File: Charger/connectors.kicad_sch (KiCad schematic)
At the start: 0 parts

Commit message: charger WIP
Most footprints assigned, shunt drawn in schem
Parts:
- added J3: Conn_01x10, symbol Connector_Generic:Conn_01x10
- added J4, J5: Conn_01x03, Connector_Molex:Molex_Micro-Fit_3.0_43650-0315_1x03_P3.00mm_Vertical, symbol Connector_Generic:Conn_01x03
- added J6, J7: Conn_01x02, Connector_Molex:Molex_Micro-Fit_3.0_43650-0215_1x02_P3.00mm_Vertical, symbol Connector_Generic:Conn_01x02
- added P1: IEC_60320_C13_Plug, symbol Connector:IEC_60320_C13_Plug
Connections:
- new net +12V: J3.6 (Pin_6), J6.2 (Pin_2)
- new net AMP_GND: J5.3 (Pin_3)
- new net AMP_SIGNAL: J5.2 (Pin_2)
- new net AMP_VCC: J5.1 (Pin_1)
- new net AMS_ERR: J3.3 (Pin_3)
- new net CANH: J3.8 (Pin_8)
- new net CANL: J3.9 (Pin_9)
- new net CAN_SHIELD: J3.10 (Pin_10)
- new net CHARGING_ENABLE: J6.1 (Pin_1)
- new net GND: J3.7 (Pin_7)
- new net GNDPWR: P1.3 (PE)
- new net IMD_ERR: J3.4 (Pin_4)
- new net LIVE: P1.2 (L)
- new net NEUT: P1.1 (N)
- new net RSNS+: J7.1 (Pin_1)
- new net RSNS-: J7.2 (Pin_2)
- new net SDC_IN: J3.2 (Pin_2)
- new net SDC_OUT: J3.1 (Pin_1)
- new net TSAL_G: J3.5 (Pin_5)
- new net VOLT_GND: J4.3 (Pin_3)
- new net VOLT_SIGNAL: J4.2 (Pin_2)
- new net VOLT_VCC: J4.1 (Pin_1)
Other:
- note added: "A control"
- note added: "J"
- note added: "MX 1x2"
- note added: "MX 1x3"
- note added: "V control"
- note added: "not fully accurate but sufficent information"

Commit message: Revise charger and HVPDU schematics
Updates the KiCad projects for Charger and Schematics with substantial schematic rework: replaces the AVR ISP header with a dedicated AVR-ISP-6 symbol, adjusts wiring/net labels and power symbols, adds new indicator/connectivity elements, and repositions components in HV iso and connector sheets. The HVPDU sheet is expanded to A3 and reorganized with additional connector/library symbol definitions and updated interconnect mapping. This commit also includes newly generated schematic backups and an exported HVPDU PDF.
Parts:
- added J10, J9: Conn_01x06, symbol Connector_Generic:Conn_01x06
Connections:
- net +12V: now also J10.1 (Pin_1)
- net GND: now also J9.1 (Pin_1), J9.2 (Pin_2), J9.3 (Pin_3), J9.4 (Pin_4), J9.5 (Pin_5), J9.6 (Pin_6)

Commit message: Charger 0.1.0 PCB ready for review
Silkscreen adjustments have not been finished yet
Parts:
- added F2: Fuse, fuse:LittleFuse_462, symbol Device:Fuse
- added H1, H2, H3, H4: MountingHole, MountingHole:MountingHole_4.3mm_M4, symbol Mechanical:MountingHole
- added J11, J12: Conn_01x02, Connector_Molex:Molex_Micro-Fit_3.0_43650-0200_1x02_P3.00mm_Horizontal, symbol Connector_Generic:Conn_01x02
- added J13, J14, J15, J16: Conn_01x02, Connector_Molex:Molex_Micro-Fit_3.0_43650-0215_1x02_P3.00mm_Vertical, symbol Connector_Generic:Conn_01x02
- added J17: Conn_01x02, Connector_JST:JST_XH_B2B-XH-A_1x02_P2.50mm_Vertical, symbol Connector_Generic:Conn_01x02
- J10, J9: footprint (none) -> Connector_Molex:Molex_Micro-Fit_3.0_43650-0615_1x06_P3.00mm_Vertical
- J7: footprint Connector_Molex:Molex_Micro-Fit_3.0_43650-0215_1x02_P3.00mm_Vertical -> Connector_Molex:Molex_Micro-Fit_3.0_43650-0200_1x02_P3.00mm_Horizontal
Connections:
- net +12V: now also J10.2 (Pin_2), J10.3 (Pin_3), J10.4 (Pin_4), J10.5 (Pin_5), J10.6 (Pin_6)
- net CANH: now also J17.2 (Pin_2)
- net CANL: now also J17.1 (Pin_1)
- net RSNS+: now also J7.2 (Pin_2); no longer J7.1 (Pin_1)
- net RSNS-: now also J7.1 (Pin_1); no longer J7.2 (Pin_2)
- net SDC_IN: now also J15.1 (Pin_1), J15.2 (Pin_2)
- new net: F2.1, J11.1 (Pin_1), J11.2 (Pin_2)
- new net CHARGER_ERR_12V: J14.1 (Pin_1), J14.2 (Pin_2)
- new net HV_ON: J13.1 (Pin_1), J13.2 (Pin_2)
- new net HV_RELAY_AUX: J16.1 (Pin_1), J16.2 (Pin_2)
- new net TS+: F2.2
- new net TS-: J12.1 (Pin_1), J12.2 (Pin_2)

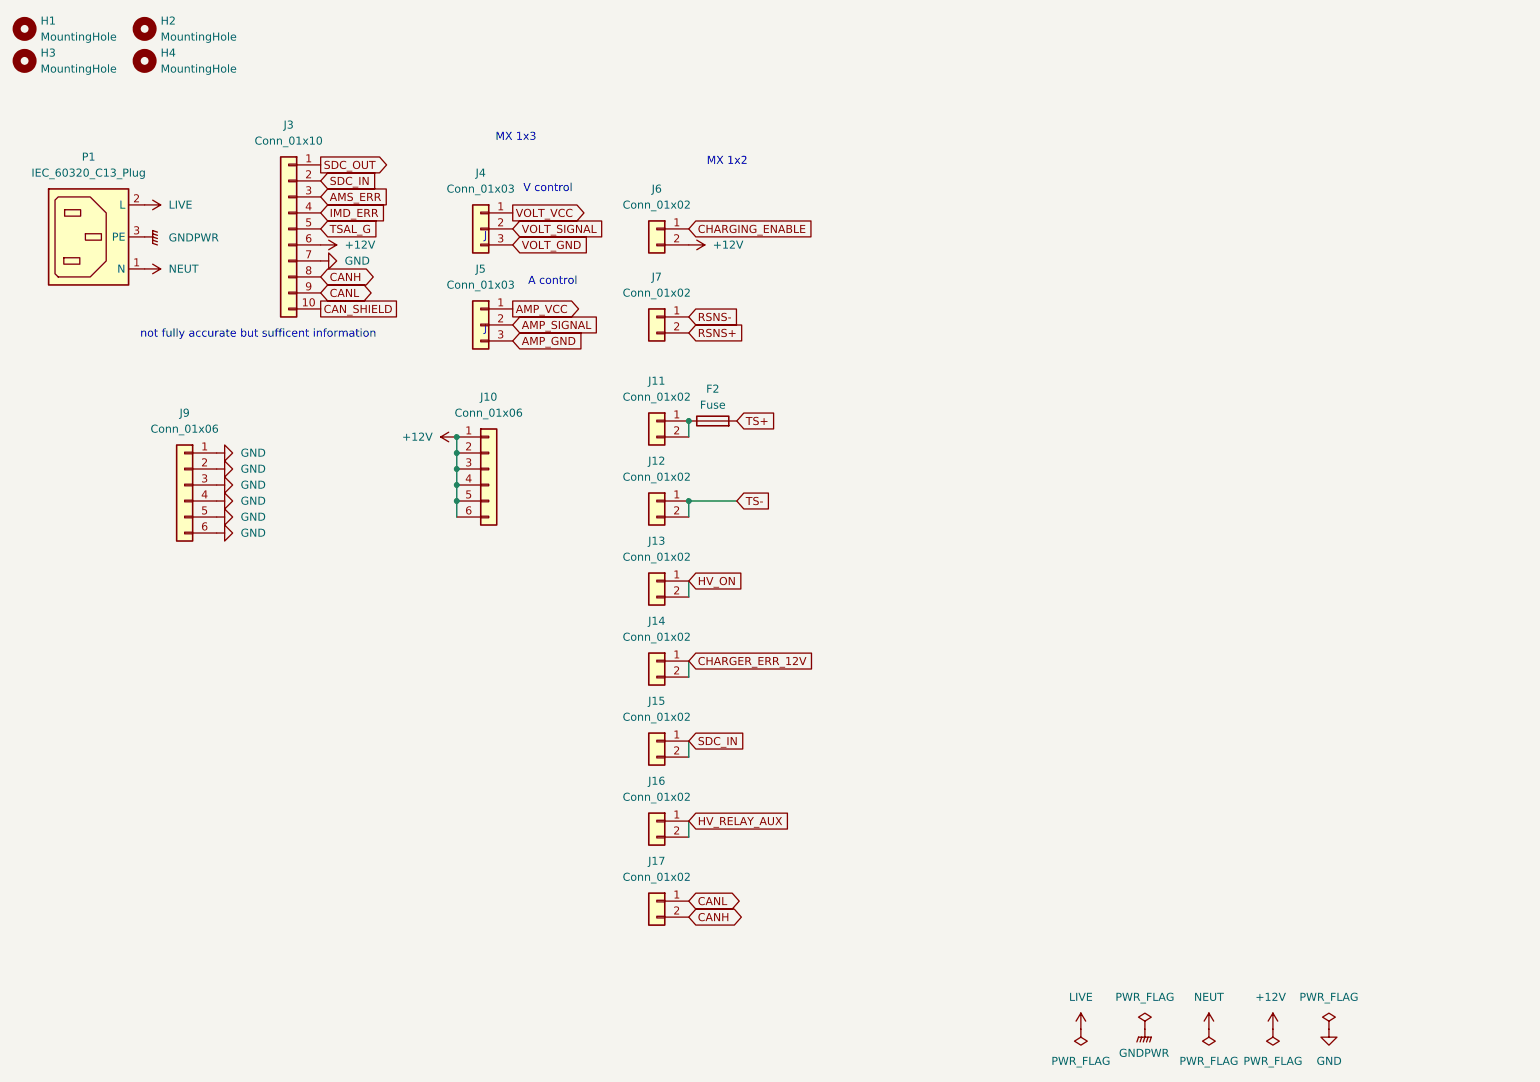
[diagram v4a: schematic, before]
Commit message: Refactor charger I/O and PCB routing
Updates the Charger KiCad project with major schematic and layout edits: reorganizes connector placement and labeling, adds new connectors J18/J19, adjusts power/ground symbols and net wiring, and reroutes key PCB nets (including CAN and oscillator traces) with small footprint position tweaks. It also updates several 3D model references to KiCad 10 STEP libraries and includes fresh Charger backup archives.
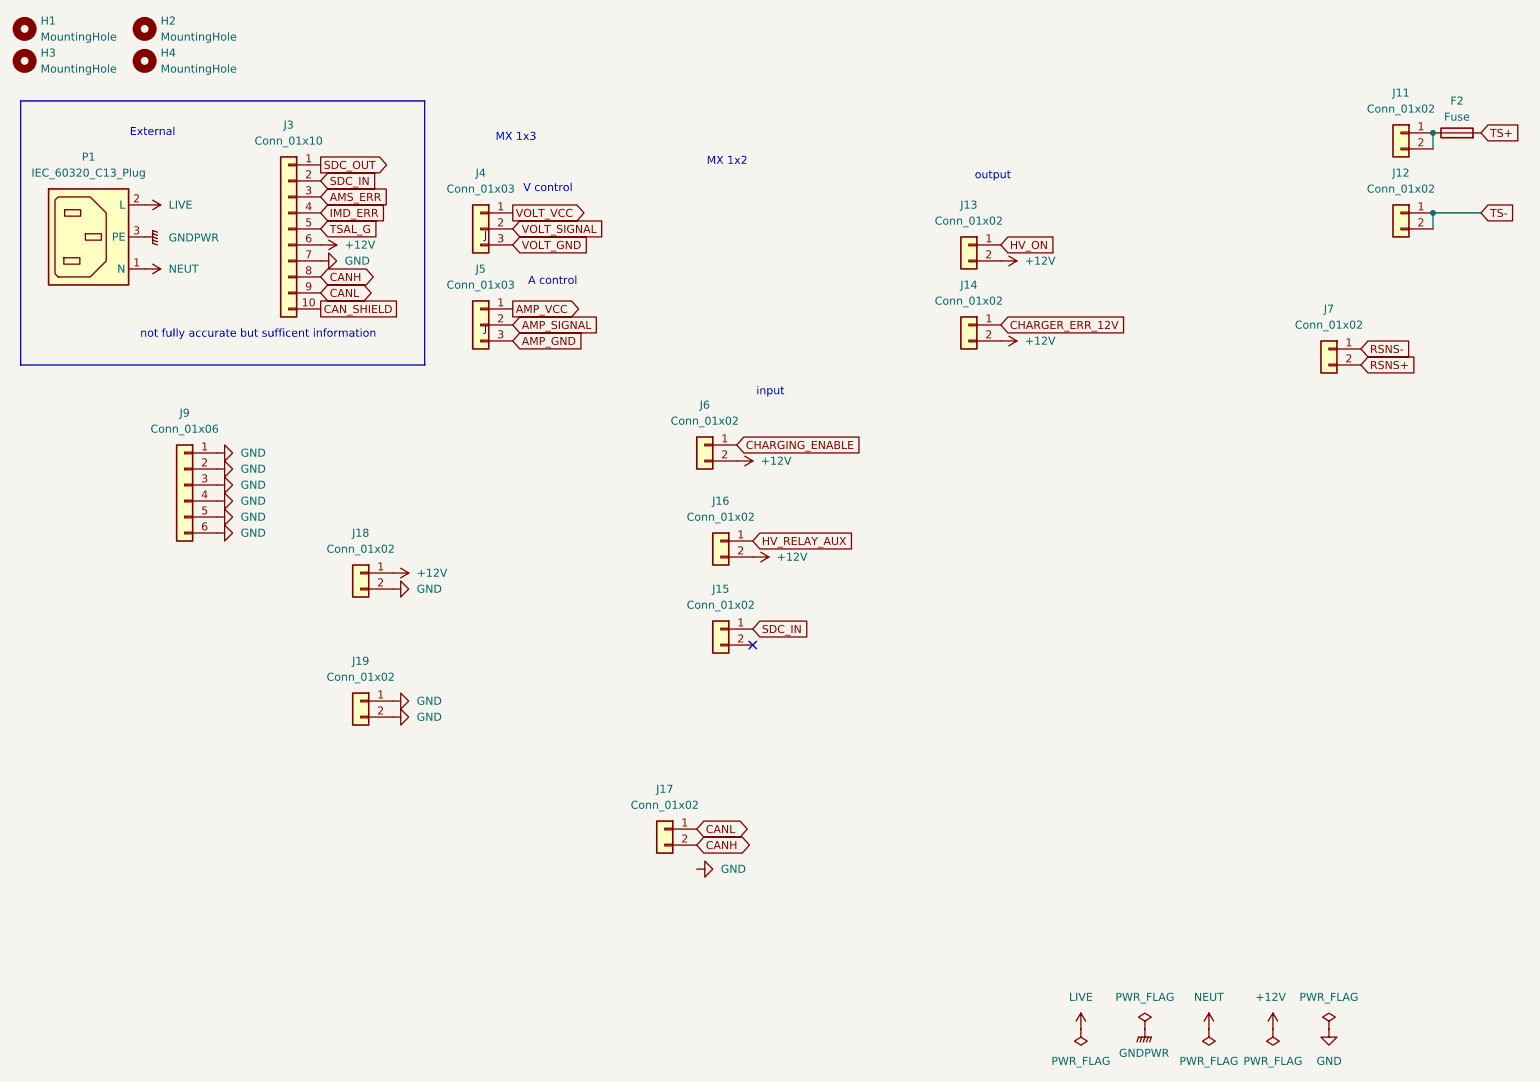
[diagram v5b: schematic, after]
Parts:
- removed J10: Conn_01x06, Connector_Molex:Molex_Micro-Fit_3.0_43650-0615_1x06_P3.00mm_Vertical, symbol Connector_Generic:Conn_01x06
- added J18, J19: Conn_01x02, Connector_Molex:Molex_Micro-Fit_3.0_43650-0215_1x02_P3.00mm_Vertical, symbol Connector_Generic:Conn_01x02
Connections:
- net +12V: now also J13.2 (Pin_2), J14.2 (Pin_2), J16.2 (Pin_2), J18.1 (Pin_1)
- net CHARGER_ERR_12V: no longer J14.2 (Pin_2)
- net GND: now also J18.2 (Pin_2), J19.1 (Pin_1), J19.2 (Pin_2)
- net HV_ON: no longer J13.2 (Pin_2)
- net HV_RELAY_AUX: no longer J16.2 (Pin_2)
- net SDC_IN: no longer J15.2 (Pin_2)
- no-connect marks 0 -> 1
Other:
- note added: "External"
- note added: "input"
- note added: "output"
- moved on the sheet: F2, J11, J12, J13, J14, J15, J16, J17, J6, J7

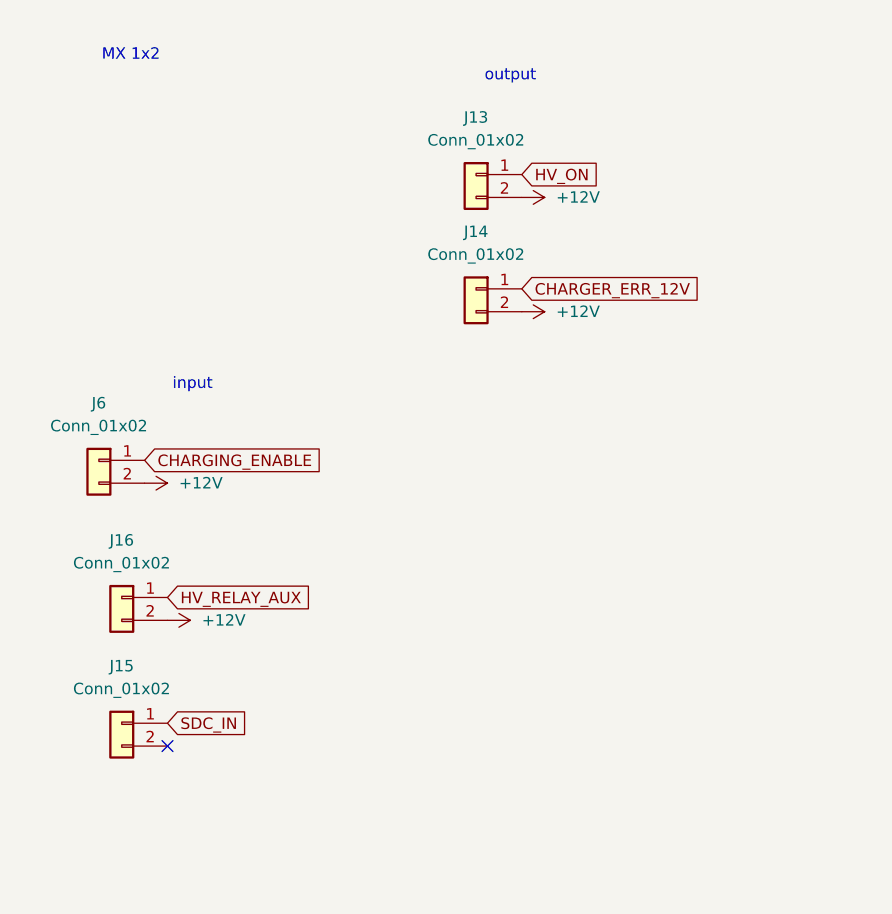
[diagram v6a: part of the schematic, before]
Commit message: Charger adjustments
silkscreen has not been readjusted fully yet
PCB adjusted to match schematic changes
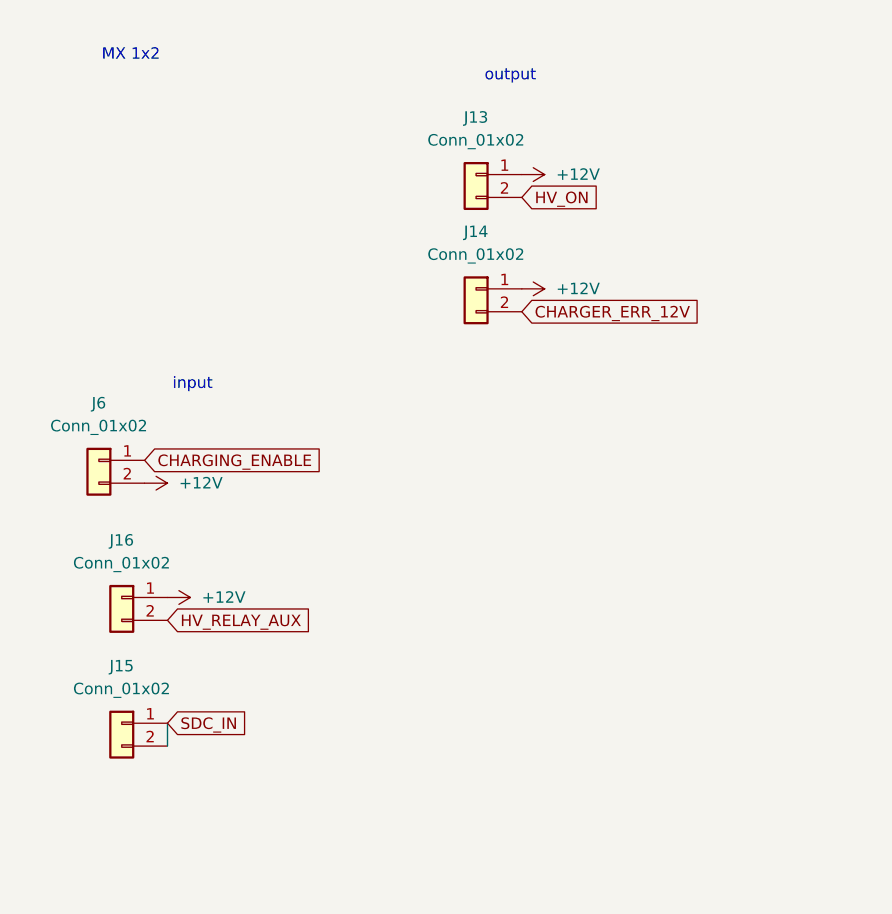
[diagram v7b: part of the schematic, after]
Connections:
- net +12V: now also J13.1 (Pin_1), J14.1 (Pin_1), J16.1 (Pin_1); no longer J13.2 (Pin_2), J14.2 (Pin_2), J16.2 (Pin_2)
- net CHARGER_ERR_12V: now also J14.2 (Pin_2); no longer J14.1 (Pin_1)
- net HV_ON: now also J13.2 (Pin_2); no longer J13.1 (Pin_1)
- net HV_RELAY_AUX: now also J16.2 (Pin_2); no longer J16.1 (Pin_1)
- net SDC_IN: now also J15.2 (Pin_2)
- no-connect marks 1 -> 0
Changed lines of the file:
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@@
 		(color 0 0 0 0)
 	)
-	(no_connect
-		(at 130.81 113.03)
-	)
 	(wire
 		(pts
@@
 	(wire
 		(pts
+			(xy 130.81 110.49) (xy 130.81 113.03)
+		)
+		(stroke
+			(width 0)
+			(type default)
+		)
+	)
+	(wire
+		(pts
 			(xy 238.76 31.75) (xy 238.76 34.29)
 		)
@@
 	(global_label "HV_RELAY_AUX"
 		(shape input)
-		(at 130.81 96.52 0)
+		(at 130.81 99.06 0)
 		(fields_autoplaced yes)
 		(effects
@@
 		)
 		(property "Intersheetrefs" "${INTERSHEET_REFS}"
-			(at 147.4024 96.52 0)
+			(at 147.4024 99.06 0)
 			(hide yes)
 			(show_name no)
@@
 	(global_label "HV_ON"
 		(shape input)
-		(at 170.18 49.53 0)
+		(at 170.18 52.07 0)
 		(fields_autoplaced yes)
 		(effects
@@
 		)
 		(property "Intersheetrefs" "${INTERSHEET_REFS}"
-			(at 179.2129 49.53 0)
+			(at 179.2129 52.07 0)
 			(hide yes)
 			(show_name no)
@@
 	(global_label "CHARGER_ERR_12V"
 		(shape input)
-		(at 170.18 62.23 0)
+		(at 170.18 64.77 0)
 		(fields_autoplaced yes)
 		(effects
@@
 		)
 		(property "Intersheetrefs" "${INTERSHEET_REFS}"
-			(at 190.9451 62.23 0)
+			(at 190.9451 64.77 0)
 			(hide yes)
 			(show_name no)
@@
 	(symbol
 		(lib_id "power:+12V")
-		(at 170.18 52.07 270)
-		(mirror x)
+		(at 170.18 49.53 270)
 		(unit 1)
 		(body_style 1)
@@
 		(dnp no)
 		(property "Reference" "#PWR0112"
-			(at 166.37 52.07 0)
+			(at 166.37 49.53 0)
 			(hide yes)
 			(show_name no)
@@
 		)
 		(property "Value" "+12V"
-			(at 173.99 52.0701 90)
+			(at 173.99 49.5299 90)
 			(show_name no)
 			(do_not_autoplace no)
@@
 		)
 		(property "Footprint" ""
-			(at 170.18 52.07 0)
+			(at 170.18 49.53 0)
 			(hide yes)
 			(show_name no)
@@
 		)
 		(property "Datasheet" ""
-			(at 170.18 52.07 0)
+			(at 170.18 49.53 0)
 			(hide yes)
 			(show_name no)
@@
 		)
 		(property "Description" "Power symbol creates a global label with name \"+12V\""
-			(at 170.18 52.07 0)
+			(at 170.18 49.53 0)
 			(hide yes)
 			(show_name no)
@@
 	(symbol
 		(lib_id "power:+12V")
-		(at 170.18 64.77 270)
-		(mirror x)
+		(at 170.18 62.23 270)
 		(unit 1)
 		(body_style 1)
@@
 		(dnp no)
 		(property "Reference" "#PWR0113"
-			(at 166.37 64.77 0)
+			(at 166.37 62.23 0)
 			(hide yes)
 			(show_name no)
@@
 		)
 		(property "Value" "+12V"
-			(at 173.99 64.7701 90)
+			(at 173.99 62.2299 90)
 			(show_name no)
 			(do_not_autoplace no)
@@
 		)
 		(property "Footprint" ""
-			(at 170.18 64.77 0)
+			(at 170.18 62.23 0)
 			(hide yes)
 			(show_name no)
@@
 		)
 		(property "Datasheet" ""
-			(at 170.18 64.77 0)
+			(at 170.18 62.23 0)
 			(hide yes)
 			(show_name no)
@@
 		)
 		(property "Description" "Power symbol creates a global label with name \"+12V\""
-			(at 170.18 64.77 0)
+			(at 170.18 62.23 0)
 			(hide yes)
 			(show_name no)
@@
 	(symbol
 		(lib_id "power:+12V")
-		(at 130.81 99.06 270)
-		(mirror x)
+		(at 130.81 96.52 270)
 		(unit 1)
 		(body_style 1)
@@
 		(dnp no)
 		(property "Reference" "#PWR0114"
-			(at 127 99.06 0)
+			(at 127 96.52 0)
 			(hide yes)
 			(show_name no)
@@
 		)
 		(property "Value" "+12V"
-			(at 134.62 99.0601 90)
+			(at 134.62 96.5199 90)
 			(show_name no)
 			(do_not_autoplace no)
@@
 		)
 		(property "Footprint" ""
-			(at 130.81 99.06 0)
+			(at 130.81 96.52 0)
 			(hide yes)
 			(show_name no)
@@
 		)
 		(property "Datasheet" ""
-			(at 130.81 99.06 0)
+			(at 130.81 96.52 0)
 			(hide yes)
 			(show_name no)
@@
 		)
 		(property "Description" "Power symbol creates a global label with name \"+12V\""
-			(at 130.81 99.06 0)
+			(at 130.81 96.52 0)
 			(hide yes)
 			(show_name no)
